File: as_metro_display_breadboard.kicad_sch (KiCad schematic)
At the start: 18 parts

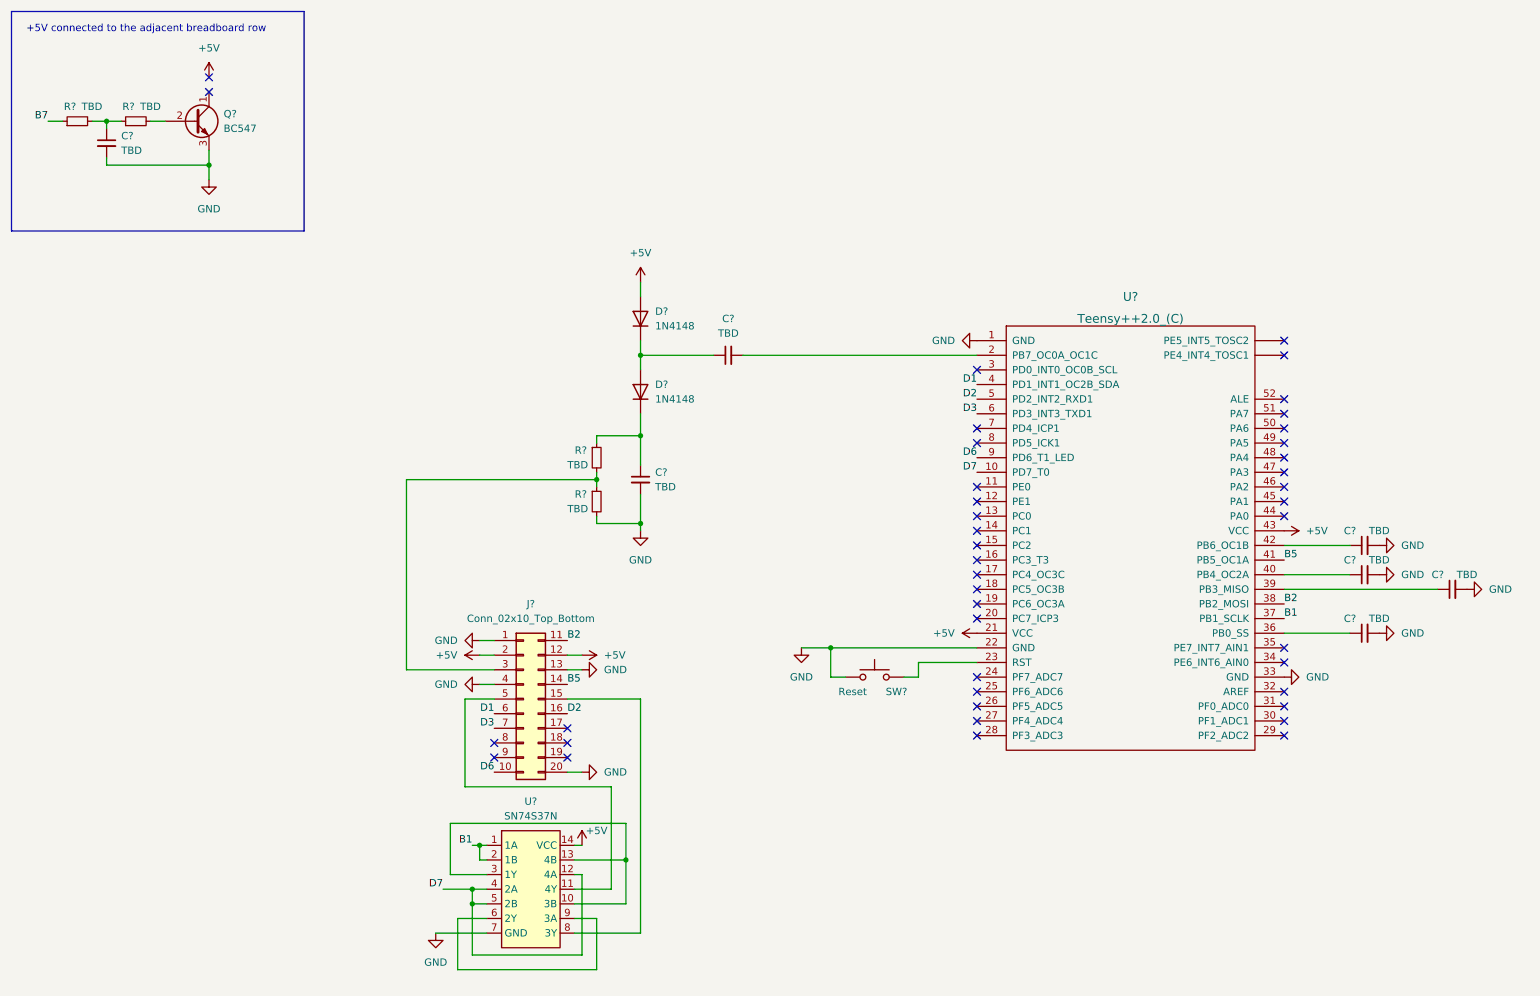
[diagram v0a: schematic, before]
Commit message: Annotate ribbon cable signals
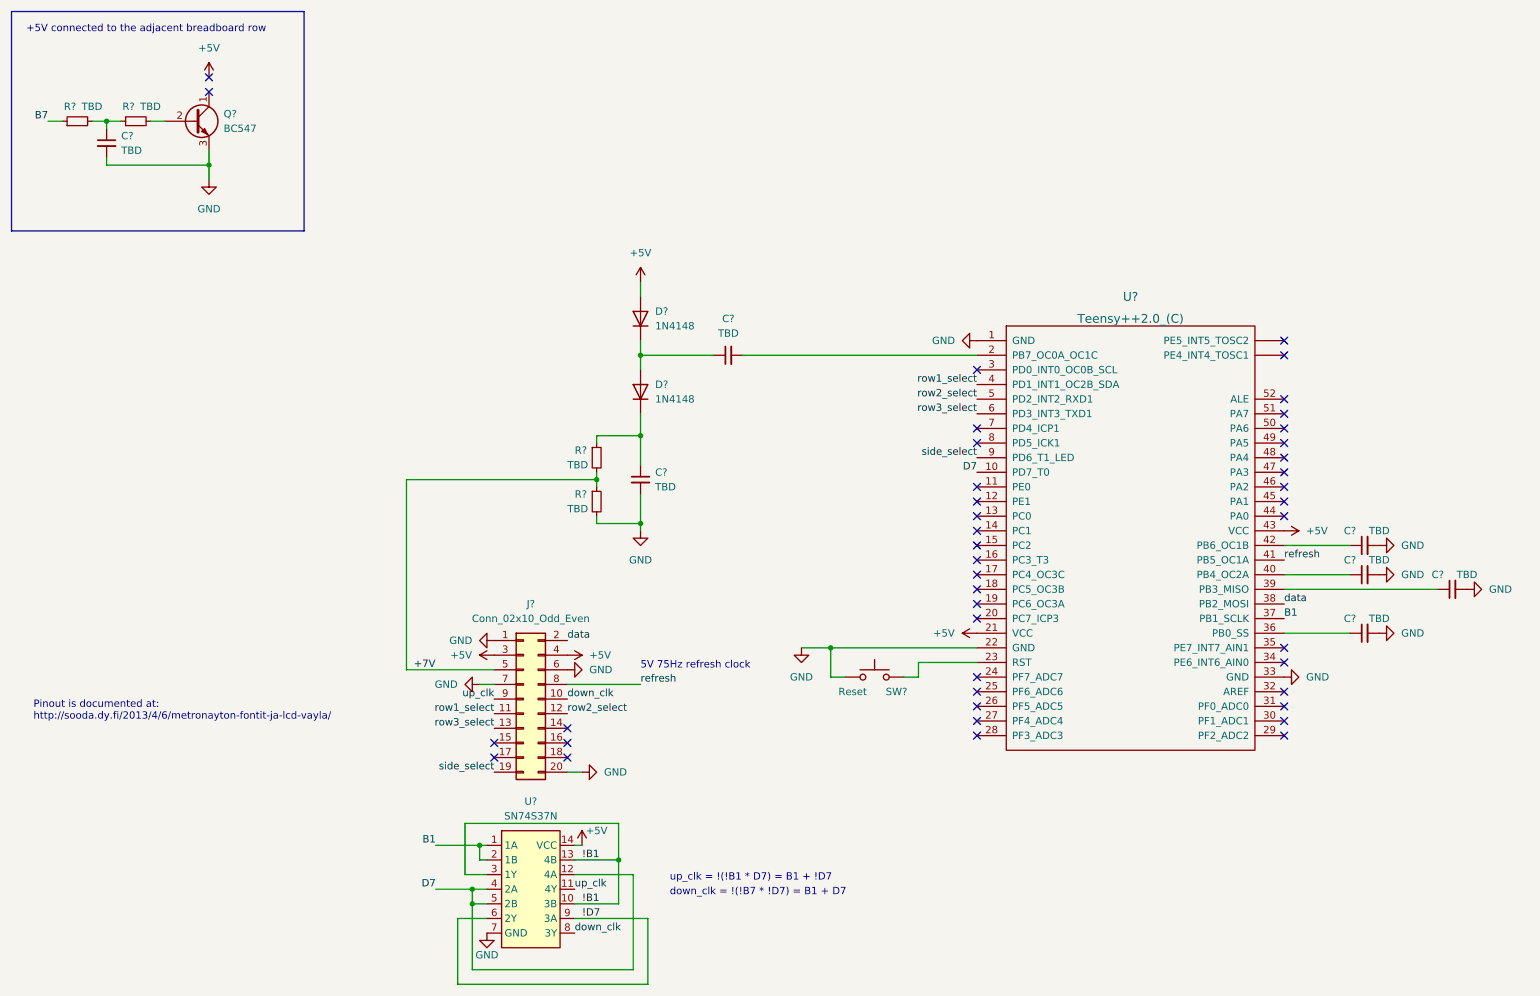
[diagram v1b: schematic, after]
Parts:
- removed J?: Conn_02x10_Top_Bottom, symbol Connector_Generic:Conn_02x10_Top_Bottom
- added J?: Conn_02x10_Odd_Even, symbol Connector_Generic:Conn_02x10_Odd_Even
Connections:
- net +5V: now also J?.3 (Pin_3), J?.4 (Pin_4)
- net GND: now also J?.1 (Pin_1), J?.20 (Pin_20), J?.6 (Pin_6), J?.7 (Pin_7)
- net +7V: now reaches R?.1, R?.2
- net +7V: now also J?.5 (Pin_5)
- net !B1: now reaches U?.10 (3B), U?.13 (4B), U?.3 (1Y)
- net up_clk: now reaches U?.11 (4Y)
- net up_clk: now also J?.9 (Pin_9)
- net !D7: now reaches U?.6 (2Y), U?.9 (3A)
- net down_clk: now reaches U?.8 (3Y)
- net down_clk: now also J?.10 (Pin_10)
- net B2 renamed data
- net data: now also J?.2 (Pin_2)
- net B5 renamed refresh
- net refresh: now also J?.8 (Pin_8)
- net D1 renamed row1_select
- net row1_select: now also J?.11 (Pin_11)
- net D2 renamed row2_select
- net row2_select: now also J?.12 (Pin_12)
- net D3 renamed row3_select
- net row3_select: now also J?.13 (Pin_13)
- net D6 renamed side_select
- net side_select: now also J?.19 (Pin_19)
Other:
- note added: "5V 75Hz refresh clock"
- note added: "Pinout is documented at: http://sooda.dy.fi/2013/4/6/metronayton-fontit-ja-lcd-vayla/"
- note added: "down_clk = !(!B7 * !D7) = B1 + D7"
- note added: "up_clk = !(!B1 * D7) = B1 + !D7"

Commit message: Annotate and add measured component values
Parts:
- removed C? (x4): TBD, symbol Device:C_Small
- added C4, C5, C6, C7: 100n, symbol Device:C_Small
- C1: renamed from C?; value TBD -> 10n
- C2, C3: renamed from C?; value TBD -> 200n
- R1: renamed from R?; value TBD -> 8.2k
- R2: renamed from R?; value TBD -> 1k
- R3: renamed from R?; value TBD -> 10k
- R4: renamed from R?; value TBD -> 27k
- gave numbers to parts that had none: 7
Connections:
- net GND: now also C4.2, C5.2, C6.2, C7.2
- net at U2.36 (PB0_SS): now also C4.1
- net at U2.39 (PB3_MISO): now also C5.1
- net at U2.40 (PB4_OC2A): now also C6.1
- net at U2.42 (PB6_OC1B): now also C7.1
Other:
- title: (none) -> AS Metro Display Breadboard
